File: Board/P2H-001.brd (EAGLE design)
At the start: 72 x 72 mm, 27 parts, among them IC1 74LS157N, IC2 LTC485N, IC3 4051N, IC4 74LS07N, IC5 LTC485N, U1 ARDUINO_PRO_MINI, U2 MAX7219DIP

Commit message: Refinement of panel and schematic.
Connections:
- net SEL0: no longer U1.A6
- net SEL1: now also U1.A6
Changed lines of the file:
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@@
 </signal>
 <signal name="SEL0">
-<contactref element="U1" pad="A6"/>
 <contactref element="IC3" pad="11"/>
 <wire x1="64.6938" y1="59.6646" x2="58.5216" y2="65.8368" width="0.254" layer="1"/>
@@
 <wire x1="42.291" y1="37.9476" x2="48.2346" y2="37.9476" width="0.254" layer="16"/>
 <wire x1="58.5216" y1="65.8368" x2="58.42" y2="66.04" width="0.254" layer="1"/>
-<wire x1="42.291" y1="37.9476" x2="42.06875" y2="37.7825" width="0.254" layer="16"/>
 <via x="51.6636" y="41.3766" extent="1-16" drill="0.6096"/>
 </signal>
 <signal name="SEL1">
-<contactref element="U1" pad="A7"/>
 <contactref element="IC3" pad="10"/>
 <wire x1="60.8076" y1="63.0936" x2="60.8076" y2="65.8368" width="0.254" layer="16"/>
@@
 <wire x1="39.5478" y1="37.9476" x2="40.6908" y2="39.0906" width="0.254" layer="16"/>
 <wire x1="60.8076" y1="65.8368" x2="60.96" y2="66.04" width="0.254" layer="16"/>
-<wire x1="39.5478" y1="37.9476" x2="39.52875" y2="37.7825" width="0.254" layer="16"/>
 <via x="57.3786" y="53.4924" extent="1-16" drill="0.6096"/>
 <via x="58.293" y="50.292" extent="1-16" drill="0.6096"/>
+<contactref element="U1" pad="A6"/>
+<contactref element="U1" pad="A7"/>
+<wire x1="40.6908" y1="39.0906" x2="42.06875" y2="37.7825" width="0" layer="19" extent="16-16"/>
+<wire x1="39.52875" y1="37.7825" x2="39.5478" y2="37.9476" width="0" layer="19" extent="16-16"/>
 </signal>
 <signal name="I2C0">

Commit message: Before the first prototyping.
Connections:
- net DIG0 renamed LIGHTPORT1
- net DIG1 renamed LIGHTPORT2
- net DIG2 renamed LIGHTPORT3
- net DIG3 renamed LIGHTPORT4
- net DIG4 renamed LIGHTPORT5
- net DIG5 renamed LIGHTPORT6
- net DIG6 renamed LIGHTPORT7
- net DIG7 renamed LIGHTPORT8
- net GDETECT renamed DETECT1
- net M0 renamed MIDI4
- net M1 renamed MIDI5
- net M2 renamed MIDI6
- net M3 renamed MIDI7
- net RXA renamed MIDI0
- net RXK renamed MIDI1
- net SWMAIN renamed S3
- net SWMAX renamed S4
- net SWMIN renamed S5
- net TXSNK renamed MIDI3
- net VDETECT renamed DETECT0
- net XDETECT renamed DETECT3
- removed net MDETECT: IC3.15, R3.2, SV1.17
- removed net N$3: R5.1, SV1.21
- removed net SEG0: CN1.9, U2.17
- removed net SEG1: CN1.10, U2.15
- removed net SEG2: CN1.11, U2.21
- removed net SEG3: CN1.12, U2.23
- removed net SEG4: CN1.13, U2.20
- removed net SEG5: CN1.14, U2.16
- removed net SEG6: CN1.15, U2.14
- removed net SEG7: CN1.16, U2.22
- removed net SEL0: IC3.11
- removed net SEL1: IC3.10, U1.A6, U1.A7
- new net DETECT2: IC3.15, R3.1, SV1.17
- new net LIGHTPORT10: CN1.10, U2.14
- new net LIGHTPORT11: CN1.11, U2.16
- new net LIGHTPORT12: CN1.12, U2.20
- new net LIGHTPORT13: CN1.13, U2.23
- new net LIGHTPORT14: CN1.14, U2.21
- new net LIGHTPORT15: CN1.15, U2.15
- new net LIGHTPORT16: CN1.16, U2.17
- new net LIGHTPORT9: CN1.9, U2.22
- new net MIDI2: R5.2, SV1.21
- new net SELECT0: IC3.11, U1.A6
- new net SELECT1: IC3.10, U1.A7
- net GND: now also R3.2; no longer R3.1
- net VCC: now also R5.1; no longer R5.2
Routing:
- net SEL0: track 74.1 -> 0.00 mm, vias 1 -> 0
- net SEG6: track 68.8 -> 0.00 mm
- net SELECT0: track 0.00 -> 68.7 mm, vias 0 -> 3
- net LIGHTPORT15: track 0.00 -> 63.9 mm
- net MDETECT: track 63.0 -> 0.00 mm
- net LIGHTPORT16: track 0.00 -> 61.3 mm
- net GND: track 349.8 -> 294.4 mm, vias 2 -> 0
- net SEG1: track 55.0 -> 0.00 mm
- net LIGHTPORT11: track 0.00 -> 52.2 mm
- net LIGHTPORT10: track 0.00 -> 51.8 mm
- net SELECT1: track 0.00 -> 50.4 mm, vias 0 -> 3
- net SEG4: track 49.6 -> 0.00 mm, vias 2 -> 0
- net SEL1: track 48.8 -> 0.00 mm, vias 2 -> 0
- net DETECT2: track 0.00 -> 47.8 mm
- net SEG0: track 47.4 -> 0.00 mm
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
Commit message: fixed many problems.
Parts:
- added JP1: (no value), pinhead:1X02
- added R8: 22k, resistor:0204/5
- R1: value 120 -> 330
- R3: value 22k -> 120
- R4: value 220 -> 22k
- R6: value 120 -> 220
- R7: value (none) -> 120
- moved R1 45.8 mm to (52.1, 52.1)
- moved R3 43.7 mm to (14.0, 26.7)
- moved R6 35.4 mm to (47.0, 52.1)
- moved R7 16.3 mm to (14.0, 39.4)
- moved R2 7.62 mm to (52.1, 34.3)
- moved R5 7.62 mm to (52.1, 26.7)
- moved R4 2.54 mm to (49.5, 52.1)
- moved U2 1.27 mm to (27.9, 62.2)
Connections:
- new net N$3: IC4.4, JP1.2
- new net N$4: JP1.1, R1.1
- net DETECT2: now also R4.1; no longer R3.1
- net GND: now also R4.2; no longer IC4.3, R3.2
- net MIDI0: now also R5.2; no longer R2.2
- net MIDI2: now also R2.2; no longer R5.2
- net MIDI3: now also R6.2; no longer R4.2
- net MIDI4: now also R3.1; no longer R1.1
- net MIDI5: now also R3.2; no longer R1.2
- net MIDI6: now also R7.1; no longer R6.1
- net MIDI7: now also R7.2; no longer R6.2
- net N$13: now also R5.1; no longer R2.1
- net N$2: now also R6.1; no longer R4.1
- net N$21: now also R8.1; no longer R7.1
- net TX: now also IC4.3
- net VCC: now also R1.2, R2.1, R8.2; no longer R5.1, R7.2
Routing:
- net MIDI6: track 131.7 -> 187.7 mm, vias 1 -> 0
- net MIDI5: track 108.7 -> 76.4 mm
- net DETECT2: track 47.8 -> 77.8 mm
- net VCC: track 280.6 -> 254.7 mm
- net SELECT1: track 50.4 -> 72.4 mm, vias 3 -> 2
- net N$3: track 0.00 -> 21.5 mm
- net VDD: track 72.9 -> 54.1 mm, vias 0 -> 1
- net LIGHTPORT16: track 61.3 -> 45.6 mm, vias 0 -> 1
- net MIDI4: track 51.9 -> 65.3 mm, vias 1 -> 0
- net LIGHTPORT6: track 48.4 -> 36.9 mm, vias 0 -> 1
- net S5: track 43.2 -> 32.5 mm, vias 1 -> 0
- net GND: track 294.4 -> 303.8 mm
- net TX: track 29.2 -> 35.8 mm
- net N$4: track 0.00 -> 6.15 mm
- net SELECT0: track 68.7 -> 62.6 mm, vias 3 -> 2
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
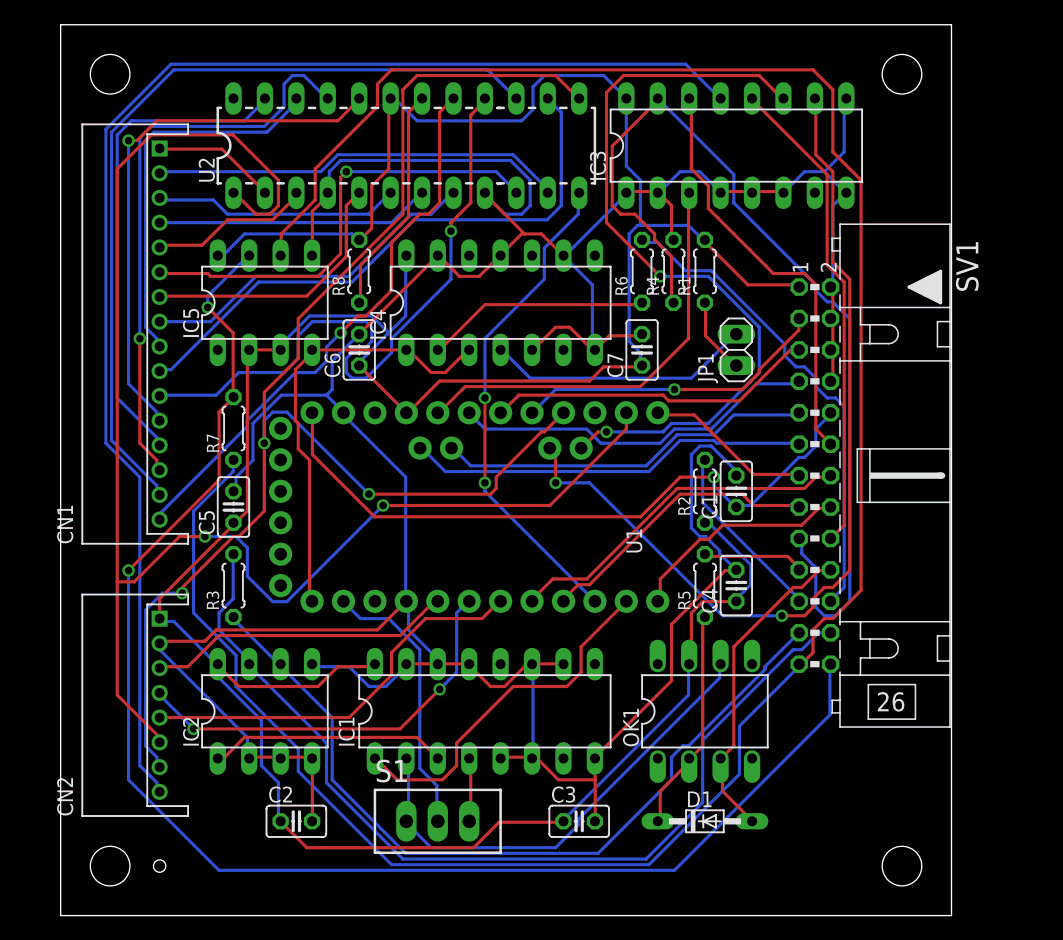
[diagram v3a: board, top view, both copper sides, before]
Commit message: Changed the positions of holes.
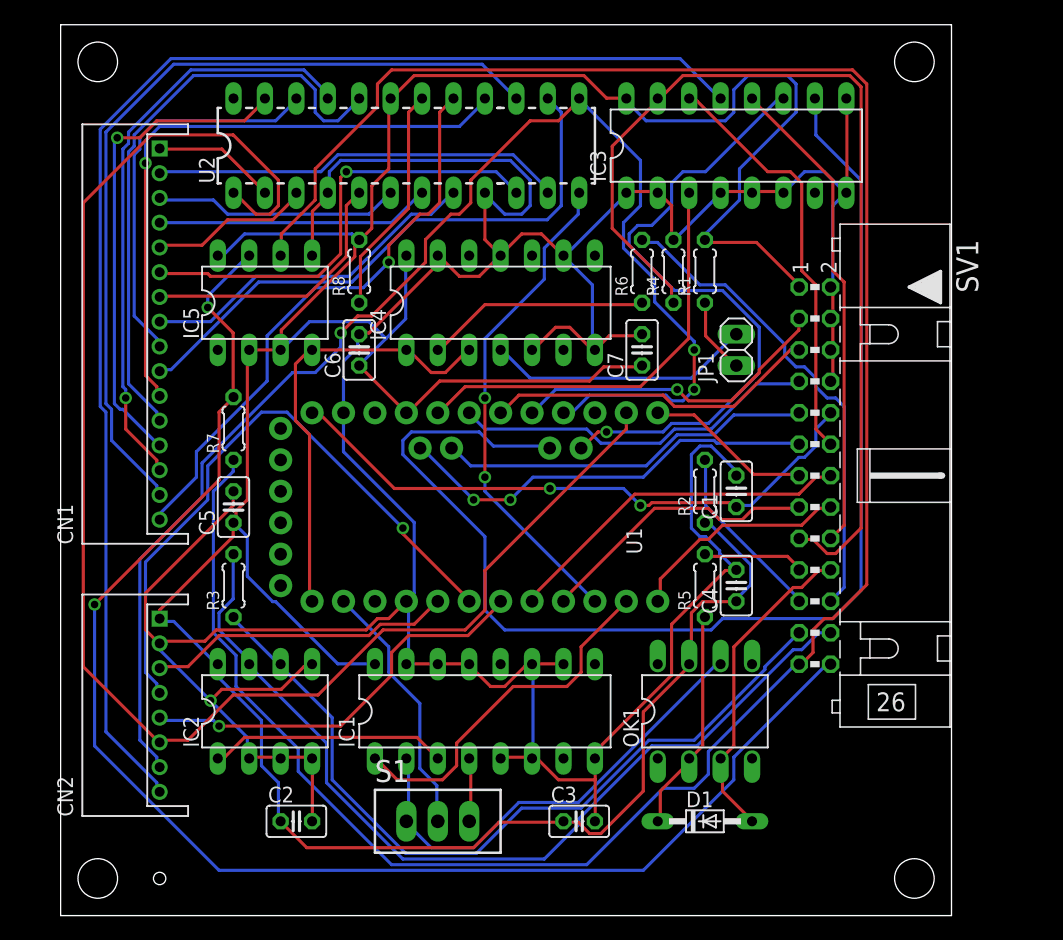
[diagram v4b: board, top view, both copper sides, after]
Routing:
- net SELECT1: track 72.4 -> 102.8 mm, vias 2 -> 0
- net VCC: track 254.7 -> 274.2 mm
- net S4: track 33.4 -> 50.6 mm, vias 2 -> 1
- net SELECT0: track 62.6 -> 52.9 mm, vias 2 -> 1
- net VDD: track 54.1 -> 49.4 mm, vias 1 -> 2
- net LIGHTPORT12: track 43.9 -> 48.0 mm, vias 1 -> 0
- net LIGHTPORT11: track 54.2 -> 50.1 mm
- net GND: track 303.8 -> 306.7 mm, vias 0 -> 1
- net MIDI5: track 76.4 -> 73.7 mm
- net I2C1: track 32.6 -> 34.5 mm, vias 0 -> 2
- net DETECT2: track 77.8 -> 79.7 mm
- net LIGHTPORT14: track 46.7 -> 48.2 mm
- net RX: track 22.3 -> 20.9 mm
- net MIDI4: track 65.3 -> 64.3 mm
- net MIDI7: track 117.2 -> 118.2 mm
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
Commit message: new panel design.
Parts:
- added LED1, LED2: (no value), led:LED3MM
- added R9: 22k, resistor:0204/5
- JP1: device pinhead:1X02 -> pinhead:1X05
- R2: value 220 -> 330
- R3, R7: value 120 -> 220
- R4, R8: value 22k -> 120
- R5: value 220 -> 22k
- moved R1 45.3 mm to (61.0, 7.62), turned to 0 degrees
- moved R4 43.7 mm to (14.0, 26.7)
- moved R3 43.4 mm to (55.9, 38.1)
- moved R7 35.4 mm to (47.0, 52.1)
- moved R6 25.7 mm to (55.9, 27.9)
- moved R5 25.5 mm to (49.5, 52.1)
- moved R2 23.3 mm to (61.0, 12.7), turned to 0 degrees
- moved R8 16.3 mm to (14.0, 39.4)
- moved C1 5.68 mm to (52.1, 39.4)
- moved JP1 3.81 mm to (54.6, 49.5)
- moved C4 2.54 mm to (52.1, 26.7)
- moved U2 1.27 mm to (26.7, 62.2)
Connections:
- new net N$5: LED1.K, R1.2
- new net N$6: LED2.K, R2.2
- net DETECT2: now also R5.1; no longer R4.1
- net GND: now also JP1.2, R5.2; no longer IC4.5, R4.2
- net I2C0: now also JP1.5
- net I2C1: now also JP1.4
- net MIDI0: now also R6.2; no longer R5.2
- net MIDI2: now also R3.2; no longer R2.2
- net MIDI3: now also R7.2; no longer R6.2
- net MIDI4: now also R4.1; no longer R3.1
- net MIDI5: now also R4.2; no longer R3.2
- net MIDI6: now also R8.1; no longer R7.1
- net MIDI7: now also R8.2; no longer R7.2
- net N$13: now also R6.1; no longer R5.1
- net N$2: now also R7.1; no longer R6.1
- net N$21: now also R9.1; no longer R8.1
- net N$3: now also R1.1; no longer JP1.2
- net N$4: now also IC4.6, R2.1; no longer JP1.1, R1.1
- net RX: now also IC4.3
- net TX: now also IC4.5; no longer IC4.3
- net VCC: now also JP1.1, LED1.A, LED2.A, R3.1, R9.2; no longer R1.2, R2.1, R8.2
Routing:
- net RX: track 20.9 -> 167.8 mm
- net N$4: track 6.15 -> 97.7 mm
- net MIDI6: track 187.4 -> 104.9 mm, vias 0 -> 3
- net S2: track 39.8 -> 100.0 mm, vias 2 -> 1
- net DETECT2: track 79.7 -> 45.1 mm, vias 0 -> 2
- net N$3: track 21.5 -> 55.8 mm, vias 0 -> 3
- net GND: track 306.7 -> 273.3 mm
- net SELECT1: track 102.8 -> 70.3 mm, vias 0 -> 1
- net I2C0: track 30.5 -> 61.0 mm, vias 0 -> 1
- net I2C1: track 34.5 -> 61.9 mm, vias 2 -> 1
- net MIDI7: track 118.2 -> 93.0 mm, vias 2 -> 0
- net VCC: track 274.2 -> 298.1 mm
- net S1: track 113.1 -> 136.0 mm, vias 3 -> 1
- net MIDI4: track 64.3 -> 85.7 mm
- net MIDI5: track 73.7 -> 92.2 mm, vias 0 -> 2
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
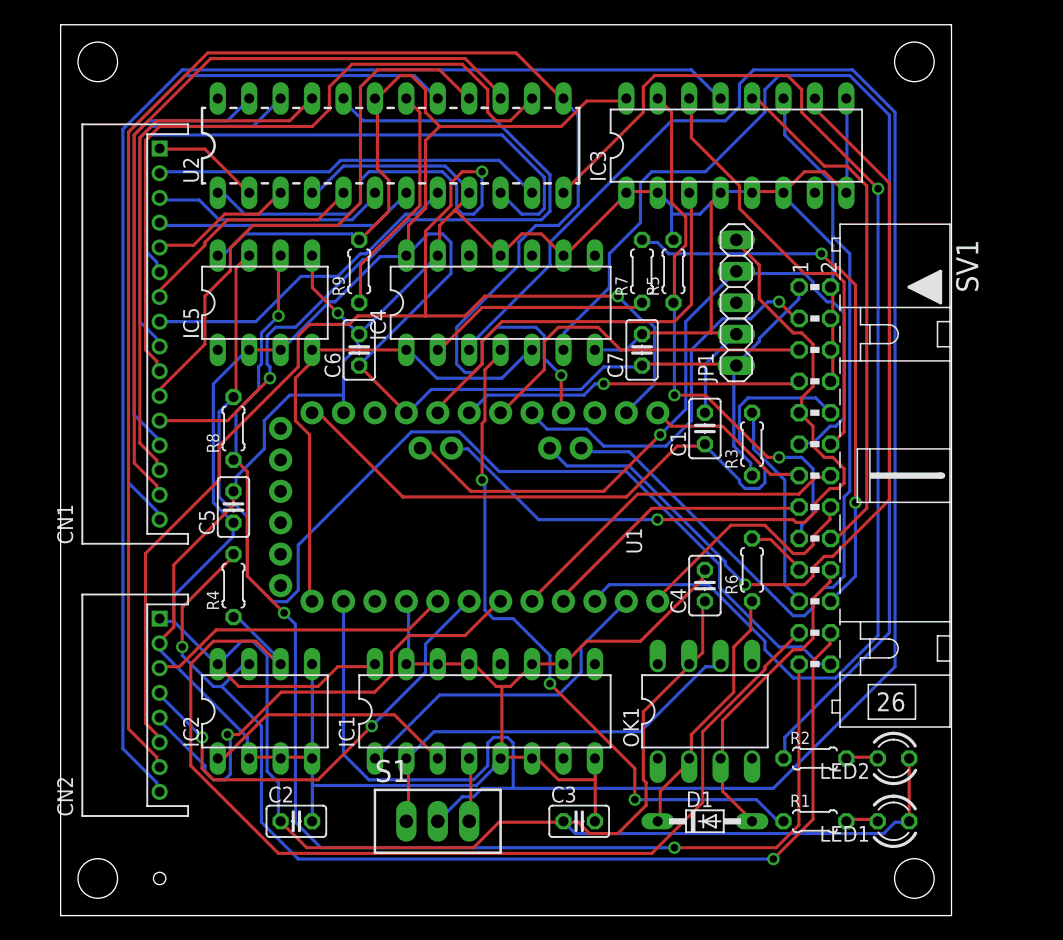
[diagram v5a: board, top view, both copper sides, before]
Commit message: Renamed files.
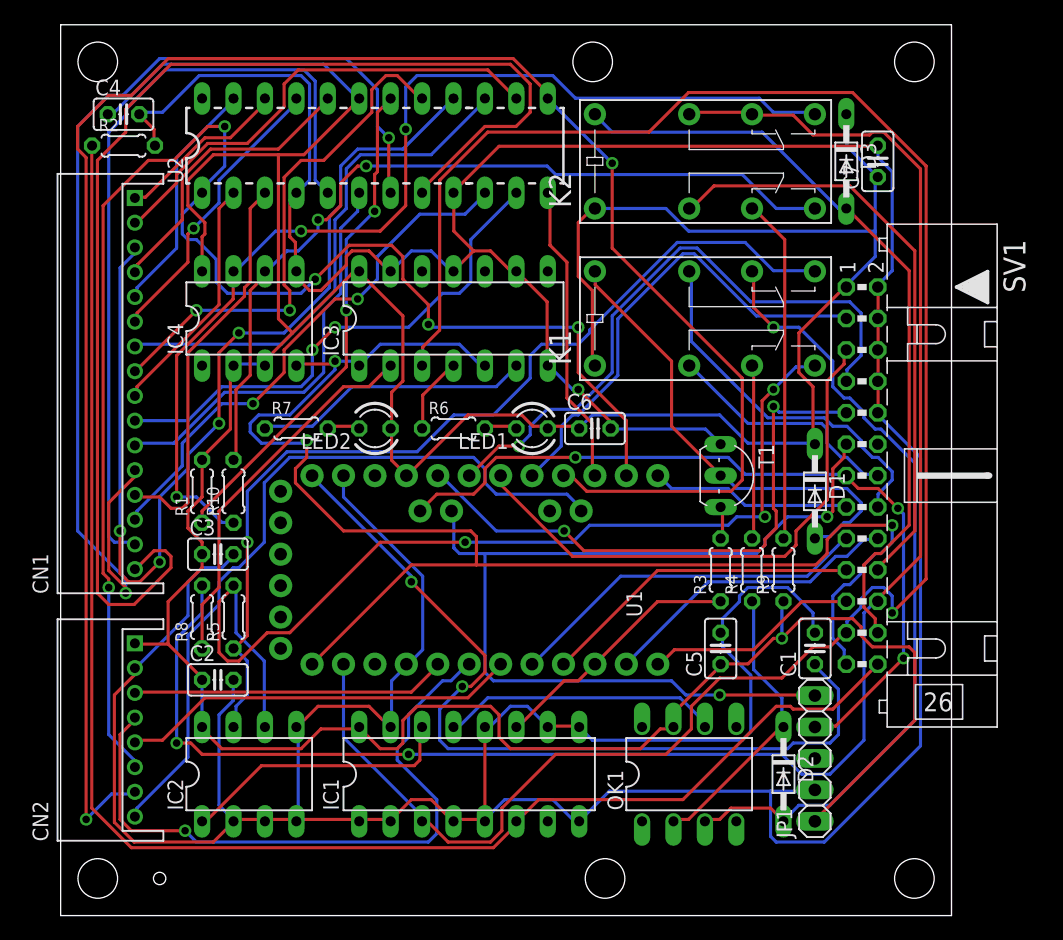
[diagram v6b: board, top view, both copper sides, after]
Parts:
- removed IC5: LTC485N, linear-technology:DIL08
- removed S1: TL39PO, switch:TL3XPO
- added D2, D3: BAS15, diode:DO34-7
- added K1, K2: G5V-2, relay:G5V-2
- added R10: 120, resistor:0204/5
- added T1: 2SC1815, transistor:TO92-ECB
- IC1: value 74LS157N -> 4051N; device 74xx-us:DIL16 -> 40xx:DIL16
- IC3: value 4051N -> 74LS07N; device 40xx:DIL16 -> 74xx-us:DIL14
- IC4: value 74LS07N -> LTC485N; device 74xx-us:DIL14 -> linear-technology:DIL08
- LED1: value (none) -> RED
- LED2: value (none) -> GRN
- R1: value 330 -> 22k
- R2: value 330 -> 10k
- R3: value 220 -> 3.3k
- R4, R8: value 120 -> 220
- R5: value 22k -> 120
- R6, R7: value 220 -> 330
- R9: value 22k -> 220
- moved R2 74.7 mm to (5.08, 62.2)
- moved C4 60.5 mm to (5.08, 64.8), turned to 0 degrees
- moved R1 56.3 mm to (11.4, 34.3), turned to 90 degrees
- moved LED2 49.7 mm to (25.4, 39.4)
- moved R5 45.2 mm to (14.0, 24.1)
- moved LED1 43.1 mm to (38.1, 39.4)
- moved R4 41.9 mm to (55.9, 27.9)
- moved R9 41.9 mm to (58.4, 27.9)
- moved C5 41.0 mm to (53.3, 21.6)
- moved JP1 37.4 mm to (61.0, 12.7)
- moved C3 36.3 mm to (12.7, 29.2)
- moved R7 30.7 mm to (19.1, 39.4), turned to 0 degrees
- moved D1 28.1 mm to (61.0, 34.3), turned to 270 degrees
- moved IC3 26.8 mm to (31.8, 48.3)
- moved R6 26.7 mm to (31.8, 39.4), turned to 0 degrees
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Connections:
- net A0 renamed IOC4
- net A1 renamed IOC5
- net A2 renamed IOC6
- net S0 renamed SYS3
- net S1 renamed SYS5
- net S3 renamed SYS0
- net S4 renamed SYS1
- net S5 renamed SYS2
- removed net ADETECT: IC3.3, U1.20
- removed net DETECT0: CN2.8, IC3.13
- removed net DETECT1: IC3.14, SV1.12
- removed net DETECT2: IC3.15, R5.1, SV1.17
- removed net DETECT3: IC3.12, SV1.18
- removed net GSELECT: SV1.13, U1.13
- removed net I2C0: JP1.5, SV1.9, U1.A4
- removed net I2C1: JP1.4, SV1.11, U1.A5
- removed net L0: SV1.14, U1.8
- removed net L1: SV1.15, U1.9
- removed net L2: SV1.16, U1.12
- removed net LIGHTPORT1: CN1.1, U2.2
- removed net LIGHTPORT10: CN1.10, U2.14
- removed net LIGHTPORT11: CN1.11, U2.16
- removed net LIGHTPORT12: CN1.12, U2.20
- removed net LIGHTPORT13: CN1.13, U2.23
- removed net LIGHTPORT14: CN1.14, U2.21
- removed net LIGHTPORT15: CN1.15, U2.15
- removed net LIGHTPORT16: CN1.16, U2.17
- removed net LIGHTPORT2: CN1.2, U2.11
- removed net LIGHTPORT3: CN1.3, U2.6
- removed net LIGHTPORT4: CN1.4, U2.7
- removed net LIGHTPORT5: CN1.5, U2.3
- removed net LIGHTPORT6: CN1.6, U2.10
- removed net LIGHTPORT7: CN1.7, U2.5
- removed net LIGHTPORT8: CN1.8, U2.8
- removed net LIGHTPORT9: CN1.9, U2.22
- removed net MIDI6: IC5.6, R8.1, SV1.25
- removed net RX: IC4.3, S1.2, U1.2
- removed net S2: U1.10, U2.12
- removed net SELECT0: IC3.11, U1.A6
- removed net SELECT1: IC3.10, U1.A7
- removed net TX: IC4.1, IC4.5, IC5.4, U1.1
- removed net XBAR: IC1.1, U1.11
- new net COM0: IC1.3, IC3.3, SV1.23, U1.2
- new net COM1: IC3.1, IC3.5, IC4.4, SV1.25, U1.1
- new net COM2: IC1.11, R3.1, U1.10
- new net COM3: SV1.18, U1.11
- new net IOC0: SV1.17, U1.8
- new net IOC1: SV1.19, U1.9
- new net IOC2: SV1.21, U1.12
- new net IOC3: SV1.15, U1.13
- new net IOC7: SV1.9, U1.20
- new net IOC8: JP1.5, SV1.11, U1.A4
- new net IOC9: JP1.4, SV1.13, U1.A5
- new net LD0: CN1.9, U2.2
- new net LD1: CN1.10, U2.11
- new net LD2: CN1.11, U2.6
- new net LD3: CN1.12, U2.7
- new net LD4: CN1.13, U2.3
- new net LD5: CN1.14, U2.10
- new net LD6: CN1.15, U2.5
- new net LD7: CN1.16, U2.8
- new net LS0: CN1.1, U2.22
- new net LS1: CN1.2, U2.14
- new net LS2: CN1.3, U2.16
- new net LS3: CN1.4, U2.20
- new net LS4: CN1.5, U2.23
- new net LS5: CN1.6, U2.21
- new net LS6: CN1.7, U2.15
- new net LS7: CN1.8, U2.17
- new net N$11: D1.A, K1.16, T1.C
- new net N$8: IC4.6, K2.8, R10.2
- new net N$9: K2.6, R9.2
- new net RX+: IC2.6, K1.8, R5.2
- new net RX-: IC2.7, K1.9, R5.1
- new net RXA: K1.6, R4.2
- new net RXK: D2.A, K1.11, OK1.3
- new net SYS4: U1.15, U2.12
- new net SYS6: CN2.8, U1.A6
- new net SYS7: U1.A7
- net GND: now also IC1.1, IC1.12, IC1.2, IC1.4, IC1.9, IC3.11, IC3.13, IC3.7, IC4.5, R2.2, SV1.10, T1.E; no longer IC1.11, IC1.13, IC1.14, IC1.6, IC3.1, IC3.2, IC3.4, IC3.5, IC3.6, IC3.8, IC4.11, IC4.13, IC4.7, IC4.9, IC5.5, R5.2
- net HSRX: now also IC1.14; no longer IC1.3
- net MIDI0: now also K1.4, SV1.14; no longer R6.2, SV1.19
- net MIDI1: now also K1.13, SV1.16; no longer D1.A, OK1.3, SV1.20
- net MIDI2: now also K2.4, SV1.20; no longer R3.2, SV1.21
- net MIDI3: now also K2.11, K2.13, R8.2; no longer R7.2
- net MIDI4: now also D3.A, K2.16, SV1.24; no longer IC2.6, R4.1, SV1.23
- net MIDI5: now also IC1.6, R2.1, SV1.26; no longer IC2.7, R4.2, SV1.24
- net MIDI7: now also IC4.7, K2.9, R10.1; no longer IC5.7, R8.2, SV1.26
- net MIDIRX: now also IC1.13; no longer IC1.2, S1.1
- net N$1: now also R3.2, T1.B; no longer IC1.4, S1.3
- net N$13: now also D2.C, R4.1; no longer D1.C, R6.1
- net N$2: now also IC3.2, R8.1; no longer IC4.2, R7.1
- net N$21: now also R1.1; no longer R9.1
- net N$3: now also IC3.4, R6.1; no longer IC4.4, R1.1
- net N$4: now also IC3.6, R7.1; no longer IC4.6, R2.1
- net N$5: now also R6.2; no longer R1.2
- net N$6: now also R7.2; no longer R2.2
- net VCC: now also D1.C, D3.C, IC3.14, IC4.2, IC4.3, IC4.8, K1.1, K2.1, R1.2, R9.1; no longer IC3.16, IC4.14, IC5.2, IC5.3, IC5.8, R3.1, R9.2
- net VDD: no longer SV1.10
- net VEE: now also IC1.7; no longer IC3.7
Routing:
- net RX: track 167.8 -> 0.00 mm
- net COM0: track 0.00 -> 164.8 mm, vias 0 -> 1
- net COM1: track 0.00 -> 121.1 mm, vias 0 -> 3
- net GND: track 273.3 -> 390.6 mm
- net DETECT0: track 106.1 -> 0.00 mm
- net MIDI6: track 104.9 -> 0.00 mm, vias 3 -> 0
- net LD7: track 0.00 -> 101.1 mm
- net S2: track 100.0 -> 0.00 mm, vias 1 -> 0
- net MIDI3: track 45.2 -> 140.3 mm
- net LD3: track 0.00 -> 87.0 mm, vias 0 -> 2
- net LS2: track 0.00 -> 82.6 mm, vias 0 -> 4
- net RX+: track 0.00 -> 82.5 mm, vias 0 -> 3
- net IOC8: track 0.00 -> 78.6 mm, vias 0 -> 2
- net RX-: track 0.00 -> 76.9 mm, vias 0 -> 1
- net N$4: track 97.7 -> 22.5 mm
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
